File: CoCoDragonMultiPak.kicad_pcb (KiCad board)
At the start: 2 copper layers, 203.2 x 203.2 mm, 51 parts, among them CN5 ATX-24, IC1 74LS245, IC10 74LS74, IC11 74LS153, IC12 74ALS30, IC13 GAL16V8, IC2 74LS367, IC3 74LS367, IC4 74LS367, IC5 74LS367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

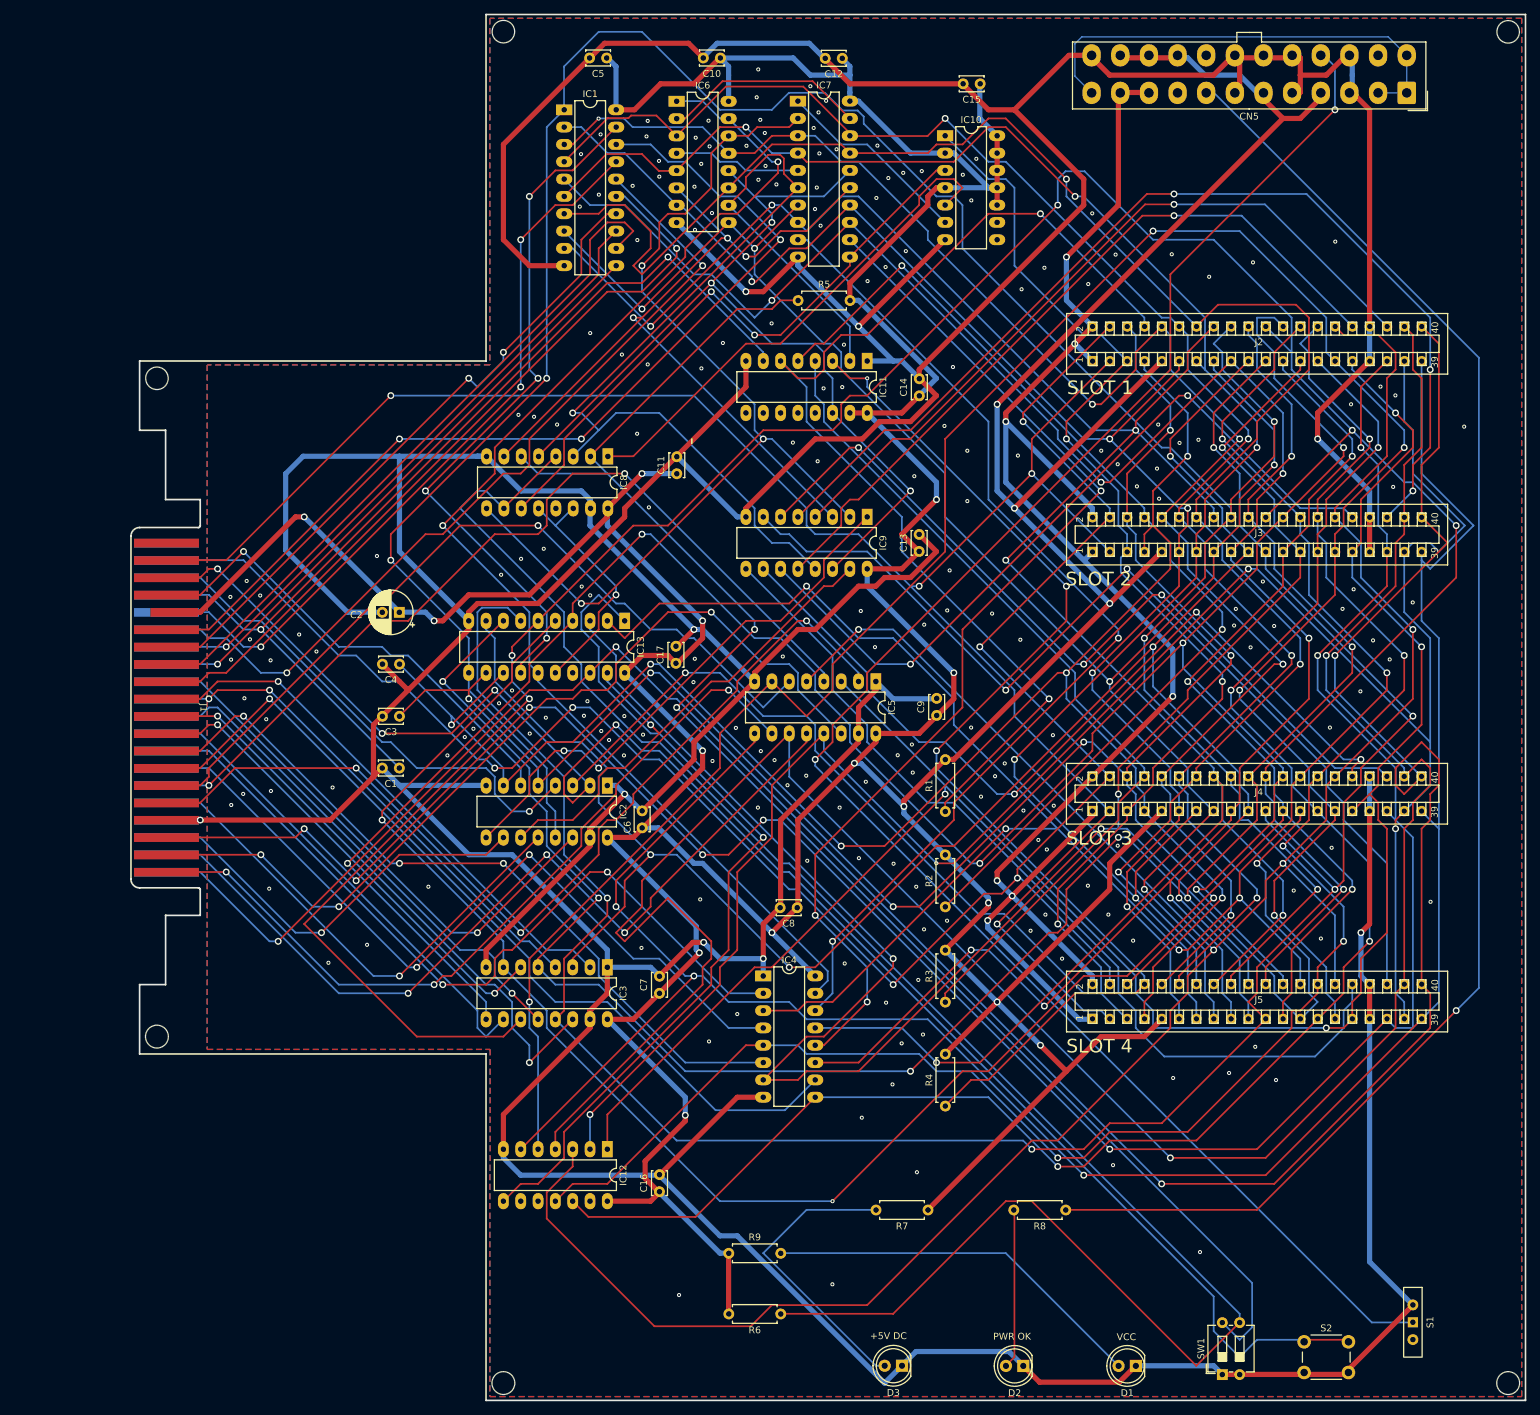
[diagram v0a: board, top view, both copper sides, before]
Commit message: convert to smd
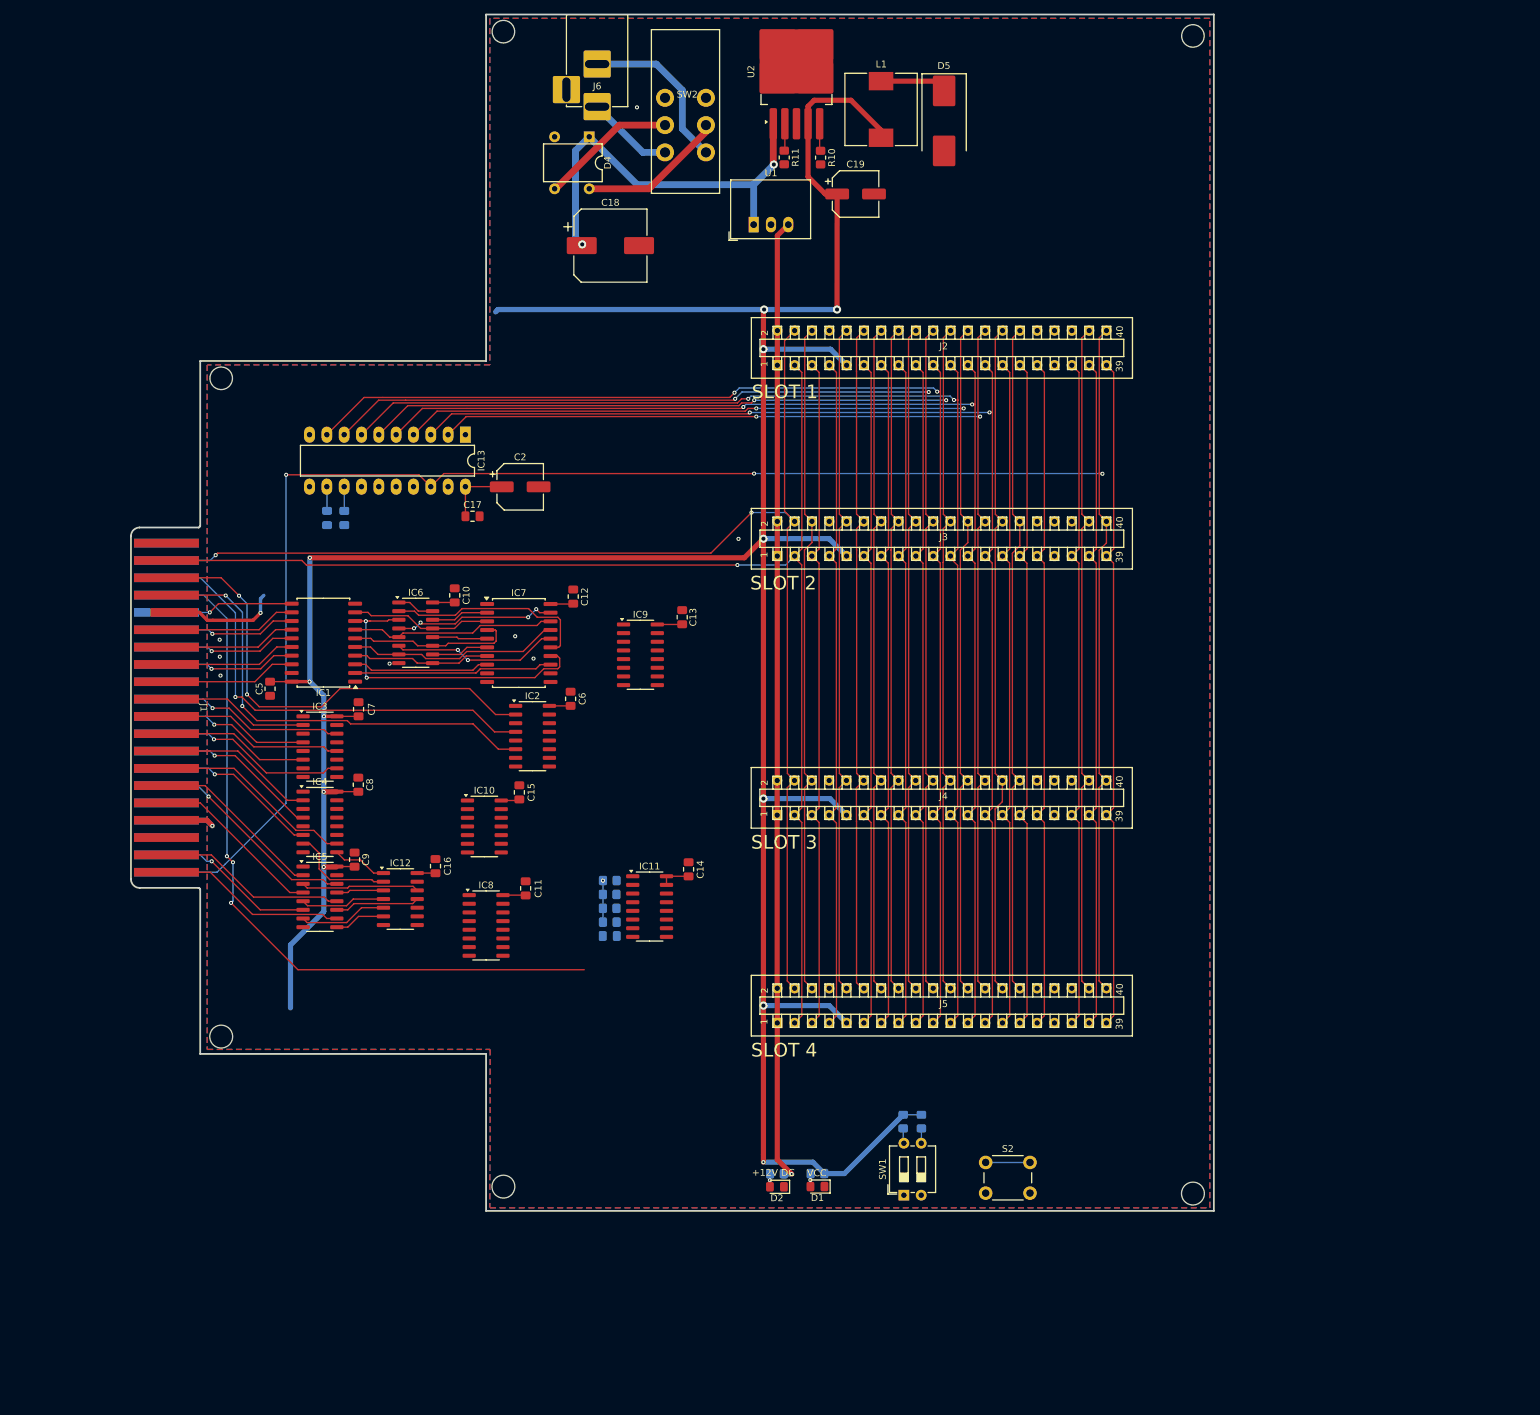
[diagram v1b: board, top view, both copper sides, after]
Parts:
- removed CN5: ATX-24, Connector_Molex:Molex_Mini-Fit_Jr_5566-24A_2x12_P4.20mm_Vertical
- removed D3: LED, LED_THT:LED_D5.0mm
- removed R7: 4.7K, Resistor_THT:R_Axial_DIN0207_L6.3mm_D2.5mm_P7.62mm_Horizontal
- removed S1: POWER, Button_Switch_THT:SW_Slide-03_Wuerth-WS-SLTV_10x2.5x6.4_P2.54mm
- added C18: 1000uF, Capacitor_SMD:CP_Elec_10x10.5, F.Cu at (120.8, 78.2)
- added C19: 220uF, Capacitor_SMD:CP_Elec_6.3x5.4_Nichicon, F.Cu at (156.8, 70.6)
- added D4: DF10G, Diode_THT:Diode_Bridge_DIP-4_W7.62mm_P5.08mm, F.Cu at (117.7, 62.2)
- added D5: MBRS340, Diode_SMD:D_SMC_Handsoldering, F.Cu at (169.7, 59.9)
- added J6: Barrel_Jack_MountingPin, CoCoDragonMultiPak:Power_BarrelJack, F.Cu at (118.9, 55.3)
- added L1: 470, Inductor_SMD:L_10.4x10.4_H4.8, F.Cu at (160.5, 58.2)
- added R10: 47K, Resistor_SMD:R_0805_2012Metric_Pad1.20x1.40mm_HandSolder, F.Cu at (151.6, 65.3)
- added R11: 47K, Resistor_SMD:R_0805_2012Metric_Pad1.20x1.40mm_HandSolder, F.Cu at (146.3, 65.3)
- added SW2: SW_DPDT_x2, CoCoDragonMultiPak:ALPS_DPDT_SPUN190900, F.Cu at (132.1, 56.5)
- added U1: R-7812-0.5, Converter_DCDC:Converter_DCDC_RECOM_R-78E-0.5_THT, F.Cu at (141.8, 75.1)
- added U2: LM2596S-5, Package_TO_SOT_SMD:TO-263-5_TabPin3, F.Cu at (148.1, 52.7)
- C1, C3, C4: value 69pF -> 68pF; footprint Capacitor_THT:C_Disc_D3.4mm_W2.1mm_P2.50mm -> Capacitor_SMD:C_0805_2012Metric_Pad1.18x1.45mm_HandSolder; moved to B.Cu
- C10, C11, C12, C13, C14, C15, C16, C17, C5, C6, C7, C8, C9: footprint Capacitor_THT:C_Disc_D3.4mm_W2.1mm_P2.50mm -> Capacitor_SMD:C_0805_2012Metric_Pad1.18x1.45mm_HandSolder
- C2: footprint Capacitor_THT:CP_Radial_D6.3mm_P2.50mm -> Capacitor_SMD:CP_Elec_6.3x5.4_Nichicon
- D1, D2: footprint LED_THT:LED_D5.0mm -> LED_SMD:LED_0805_2012Metric_Pad1.15x1.40mm_HandSolder
- IC1: value 74LS245 -> 74LS245DWR; footprint Package_DIP:DIP-20_W7.62mm_LongPads -> Package_SO:SOIC-20W_7.5x12.8mm_P1.27mm
- IC10: value 74LS74 -> 74LS74ADR; footprint Package_DIP:DIP-14_W7.62mm_LongPads -> Package_SO:SOIC-14_3.9x8.7mm_P1.27mm
- IC11: value 74LS153 -> 74LS153DR; footprint Package_DIP:DIP-16_W7.62mm_LongPads -> Package_SO:SOIC-16_3.9x9.9mm_P1.27mm
- IC12: value 74ALS30 -> 74ALS30ADR; footprint Package_DIP:DIP-14_W7.62mm_LongPads -> Package_SO:SOIC-14_3.9x8.7mm_P1.27mm
- IC2, IC3, IC4, IC5, IC6: value 74LS367 -> 74LS367ADR; footprint Package_DIP:DIP-16_W7.62mm_LongPads -> Package_SO:SOIC-16_3.9x9.9mm_P1.27mm
- IC7: value 74LS374 -> 74LS374DWR; footprint Package_DIP:DIP-20_W7.62mm_LongPads -> Package_SO:SOIC-20W_7.5x12.8mm_P1.27mm
- IC8: value 74LS368 -> 74LS368AD; footprint Package_DIP:DIP-16_W7.62mm_LongPads -> Package_SO:SOIC-16_3.9x9.9mm_P1.27mm
- IC9: value 74LS139 -> 74LS139ADR; footprint Package_DIP:DIP-16_W7.62mm_LongPads -> Package_SO:SOIC-16_3.9x9.9mm_P1.27mm
- R1, R2, R3, R4, R5, R6, R8, R9: footprint Resistor_THT:R_Axial_DIN0207_L6.3mm_D2.5mm_P7.62mm_Horizontal -> Resistor_SMD:R_0805_2012Metric_Pad1.20x1.40mm_HandSolder; moved to B.Cu
- moved C15 123.9 mm to (107.5, 158.3), turned to 90 degrees
- moved IC10 121.7 mm to (102.3, 163.3)
- moved R5 121.4 mm to (163.7, 206.6), turned to 90 degrees
- moved C5 104.8 mm to (70.9, 143.2), turned to -90 degrees
- moved IC7 89.4 mm to (107.4, 136.4)
- moved C12 88.2 mm to (115.4, 129.6), turned to 90 degrees
- moved C9 87.9 mm to (83.3, 168.2)
- moved C10 87.9 mm to (98.0, 129.5), turned to 90 degrees
- moved IC5 87.4 mm to (78.2, 173.7), turned to 0 degrees
- moved IC6 86.8 mm to (92.3, 135.0)
- moved IC11 86.1 mm to (126.6, 175.1), turned to 0 degrees
- moved IC1 85.7 mm to (78.7, 136.4), turned to 180 degrees
- moved C14 77.2 mm to (132.3, 169.6)
- moved IC8 71.0 mm to (102.6, 177.9), turned to 0 degrees
- moved IC4 68.8 mm to (78.2, 162.7)
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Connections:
- IC1 pad 11: /D6 -> /D0
- IC1 pad 12: /D5 -> /D1
- IC1 pad 13: /D4 -> /D2
- IC1 pad 15: /D7 -> /D4
- IC1 pad 16: /D2 -> /D5
- IC1 pad 17: /D0 -> /D6
- IC1 pad 18: /D1 -> /D7
- IC1 pad 2: /ID1 -> /ID7
- IC1 pad 3: /ID0 -> /ID6
- IC1 pad 4: /ID2 -> /ID5
- IC1 pad 5: /ID7 -> /ID4
- IC1 pad 7: /ID4 -> /ID2
- IC1 pad 8: /ID5 -> /ID1
- IC1 pad 9: /ID6 -> /ID0
- IC12 pad 1: /IA12 -> /IA8
- IC12 pad 11: /IA9 -> /IA13
- IC12 pad 12: /IA8 -> /IA10
- IC12 pad 2: /IA13 -> /IA9
- IC12 pad 4: /IA14 -> /IA12
- IC12 pad 5: /IA10 -> /IA14
- IC3 pad 13: /IA2 -> /IA1
- IC3 pad 14: /A2 -> /A1
- IC3 pad 4: /A1 -> /A2
- IC3 pad 5: /IA1 -> /IA2
- IC4 pad 2: /A7 -> /A6
- IC4 pad 3: /IA7 -> /IA6
- IC4 pad 4: /A9 -> /A7
- IC4 pad 5: /IA9 -> /IA7
- IC4 pad 6: /A6 -> /A9
- IC4 pad 7: /IA6 -> /IA9
- IC5 pad 11: /IA14 -> /IA13
- IC5 pad 12: /A14 -> /A13
- IC5 pad 13: /IA13 -> /IA11
- IC5 pad 14: /A13 -> /A11
- IC5 pad 2: /A12 -> /A10
- IC5 pad 3: /IA12 -> /IA10
- IC5 pad 4: /A11 -> /A12
- IC5 pad 5: /IA11 -> /IA12
- IC5 pad 6: /A10 -> /A14
- IC5 pad 7: /IA10 -> /IA14
- IC6 pad 11: /ID4 -> /ID3
- IC6 pad 12: /REGC0 -> /CK1
- IC6 pad 2: /CK0 -> /REGS1
- IC6 pad 3: /ID2 -> /ID1
- IC6 pad 4: /CK1 -> /CK0
- IC6 pad 5: /ID3 -> /ID2
- IC6 pad 6: /REGS1 -> /REGC0
- IC6 pad 7: /ID1 -> /ID4
- J1 pad 9: +5V -> +5VA
- R8 pad 1: /PWR_OK -> +12V
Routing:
- net GND: track 1267.8 -> 14.1 mm, vias 216 -> 9
- net +5V: track 964.5 -> 501.7 mm, vias 18 -> 13
- net /IR/~{W}: track 395.7 -> 99.1 mm, vias 5 -> 0
- net /DEFAULT1: track 275.0 -> 2.19 mm
- net /PS_ON: track 258.2 -> 0.00 mm, vias 2 -> 0
- net /IA11: track 363.8 -> 106.1 mm, vias 4 -> 0
- net /EXTSND: track 349.3 -> 99.1 mm, vias 8 -> 0
- net /IA14: track 348.9 -> 112.0 mm, vias 2 -> 0
- net /DEFAULT0: track 237.3 -> 2.22 mm, vias 2 -> 0
- net /IA10: track 344.6 -> 116.4 mm, vias 5 -> 0
- net /ID6: track 344.8 -> 119.1 mm, vias 6 -> 0
- net /PWR_OK: track 222.4 -> 0.00 mm, vias 1 -> 0
- net /IA15: track 326.0 -> 106.6 mm, vias 3 -> 0
- net /IA3: track 403.7 -> 184.8 mm, vias 6 -> 2
- net /IA13: track 314.0 -> 111.5 mm, vias 4 -> 0
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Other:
- board size 203.2 x 203.2 mm -> 148.6 x 175.4 mm
- board text added: "+12V DC"
- board text removed: "+5V DC"
- board text removed: "PWR OK"

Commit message: progress trace routing
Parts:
- C3, C4: moved to F.Cu
- moved C15 45.1 mm to (119.9, 201.7)
- moved IC10 45.1 mm to (114.8, 206.7)
- moved IC8 36.4 mm to (125.5, 206.1)
- moved C11 36.4 mm to (131.3, 200.7)
- moved C14 29.9 mm to (119.9, 196.8), turned to -90 degrees
- moved R4 26.2 mm to (131.5, 195.2), turned to 0 degrees
- moved R3 22.6 mm to (131.5, 193.1), turned to 0 degrees
- moved R2 19.1 mm to (131.5, 191.1), turned to 0 degrees
- moved IC11 16.3 mm to (125.7, 191.4), turned to 180 degrees
- moved R1 15.9 mm to (131.5, 189.1), turned to 0 degrees
- moved C1 13.2 mm to (131.5, 187.0), turned to 0 degrees
- moved C13 11.9 mm to (131.3, 144.6)
- moved IC9 11.9 mm to (125.2, 150.1)
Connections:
- J1 pad 9: +5VA -> +5V
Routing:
- net /EXTSND: track 99.1 -> 246.3 mm, vias 0 -> 4
- net +5V: track 501.7 -> 626.8 mm, vias 13 -> 24
- net /~{CART1}: track 0.00 -> 120.5 mm, vias 0 -> 2
- net /IA15: track 106.6 -> 214.0 mm, vias 0 -> 2
- net /IA14: track 112.0 -> 215.7 mm, vias 0 -> 2
- net /IA13: track 111.5 -> 211.8 mm, vias 0 -> 2
- net /IA12: track 111.5 -> 210.3 mm, vias 0 -> 4
- net /IA11: track 106.1 -> 199.9 mm, vias 0 -> 2
- net /IA8: track 107.2 -> 200.4 mm, vias 0 -> 2
- net /~{CART2}: track 0.00 -> 93.1 mm, vias 0 -> 2
- net /IA9: track 114.5 -> 205.8 mm, vias 0 -> 2
- net /IA10: track 116.4 -> 206.6 mm, vias 0 -> 2
- net /IA7: track 178.5 -> 265.8 mm, vias 2 -> 3
- net /IA6: track 182.8 -> 263.8 mm, vias 2 -> 3
- net /FFxx: track 0.00 -> 77.3 mm, vias 0 -> 1
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
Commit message: finish routing
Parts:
- moved C13 20.8 mm to (115.6, 158.1)
- moved IC9 20.8 mm to (109.4, 163.6)
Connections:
- IC8 pad 13: unconnected-(IC8-O6b-Pad13) -> /REGC1
- IC8 pad 14: /CTRL1 -> /DEFAULT0
- IC8 pad 2: /DEFAULT0 -> /CTRL1
- IC8 pad 3: /REGC1 -> unconnected-(IC8-O1a-Pad3)
- IC8 pad 4: /DEFAULT1 -> /DEFAULT0
- IC8 pad 5: /REGC0 -> /REGS1
- IC8 pad 6: /DEFAULT0 -> /DEFAULT1
- IC8 pad 7: /REGS1 -> /REGC0
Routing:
- net /~{P21}: track 0.00 -> 151.9 mm, vias 0 -> 1
- net /~{CTS1}: track 0.00 -> 142.0 mm, vias 0 -> 1
- net /REGS0: track 8.42 -> 149.5 mm, vias 0 -> 4
- net /~{P22}: track 0.00 -> 134.9 mm, vias 0 -> 3
- net /CTRL1: track 0.00 -> 131.7 mm, vias 0 -> 4
- net /~{RESET}: track 76.0 -> 200.4 mm, vias 2 -> 6
- net /~{CTS2}: track 0.00 -> 123.8 mm, vias 0 -> 3
- net /I~{RESET}: track 99.1 -> 220.3 mm, vias 0 -> 4
- net +5V: track 626.8 -> 737.2 mm, vias 24 -> 33
- net /LOADREG: track 0.00 -> 104.9 mm, vias 0 -> 2
- net /~{P24}: track 0.00 -> 102.9 mm, vias 0 -> 1
- net /REGS1: track 30.4 -> 129.8 mm, vias 0 -> 6
- net /REGC1: track 8.42 -> 105.9 mm, vias 0 -> 6
- net /~{P23}: track 0.00 -> 97.2 mm, vias 0 -> 3
- net /IR/~{W}: track 132.2 -> 226.1 mm, vias 2 -> 7
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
